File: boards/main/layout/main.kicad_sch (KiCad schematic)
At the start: 31 parts, among them IC1 STM32H725RGV6, P1 BM05B-SRSS-TB(LF)(SN)

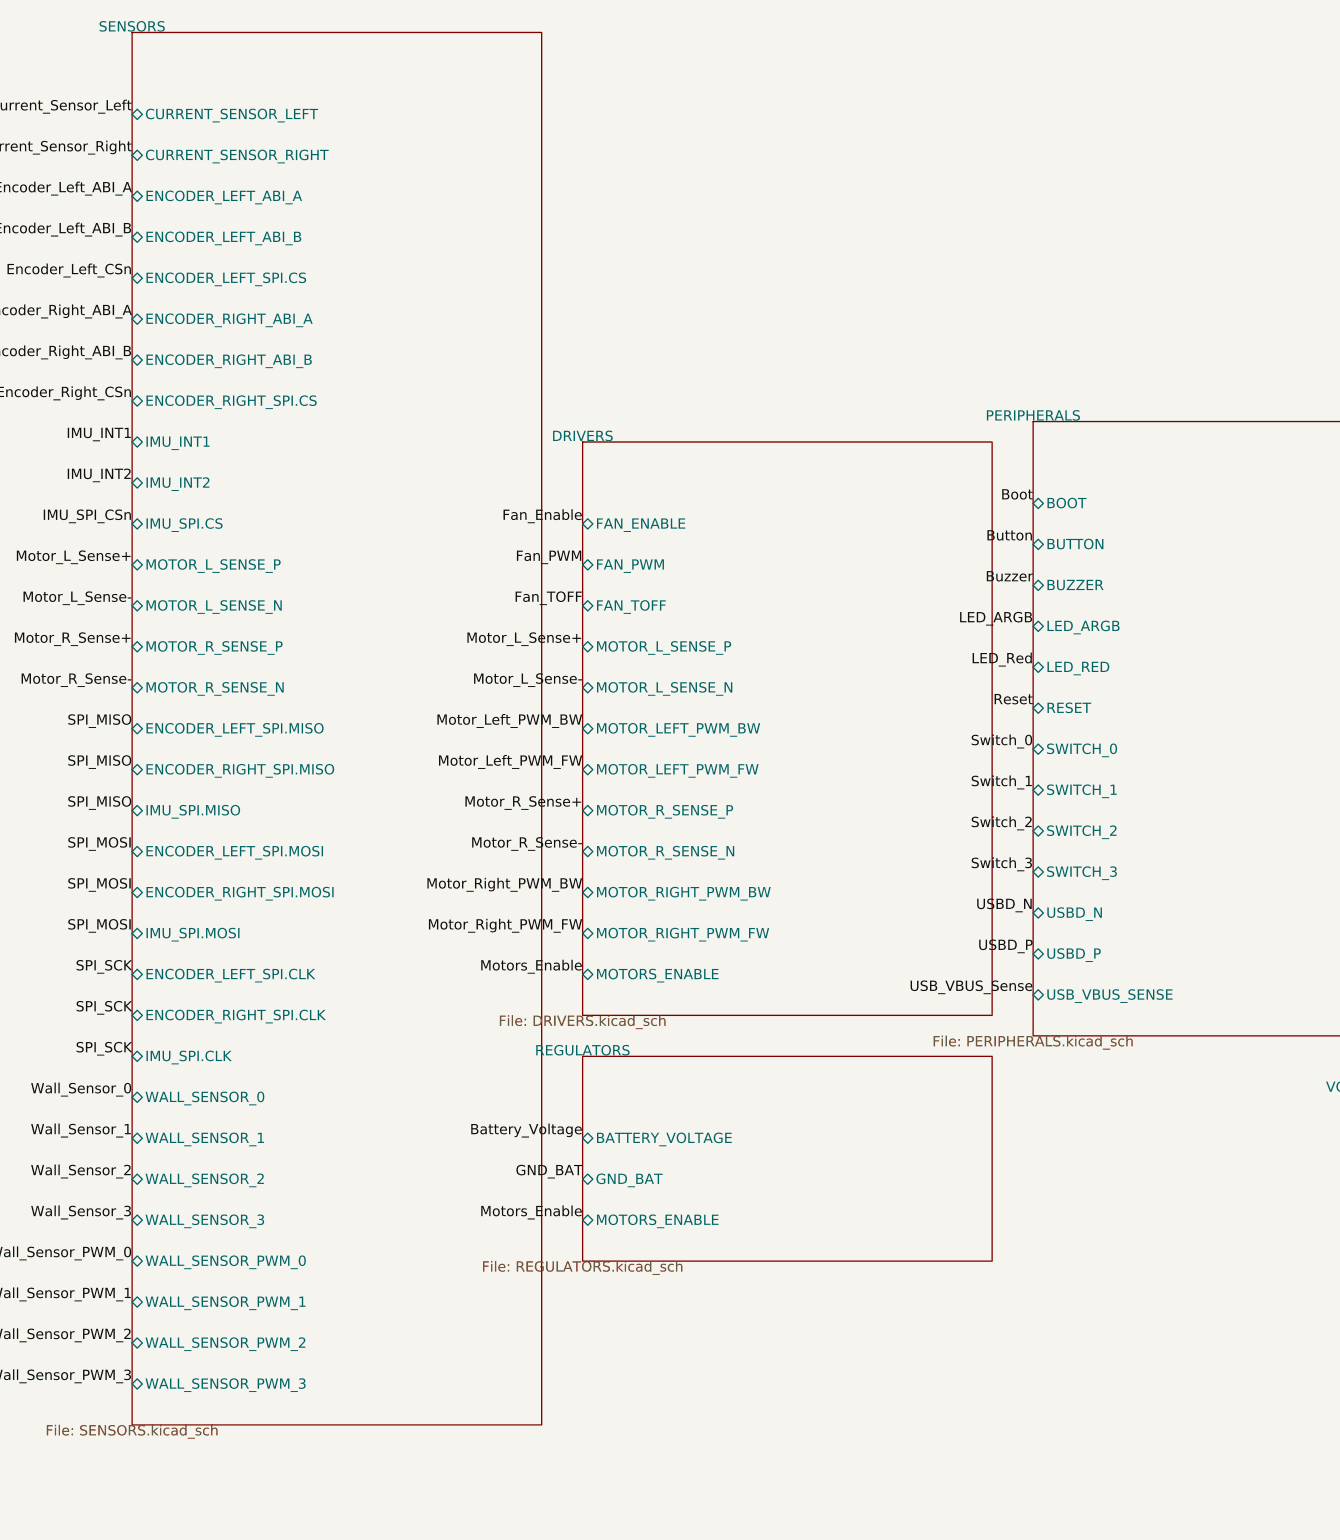
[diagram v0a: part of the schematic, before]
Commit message: 🏷️ Name the main board's module ports after their nets
A sheet pin and its hierarchical label take the module's port name and the root's label the net
name; KiCad's ERC flagged the 33 nets whose two names differed only in case (similar_labels).
GND_BAT becomes a ground port of REGULATORS, so the root shows a power symbol at its sheet pin
instead of a label nothing else joined (label_dangling).
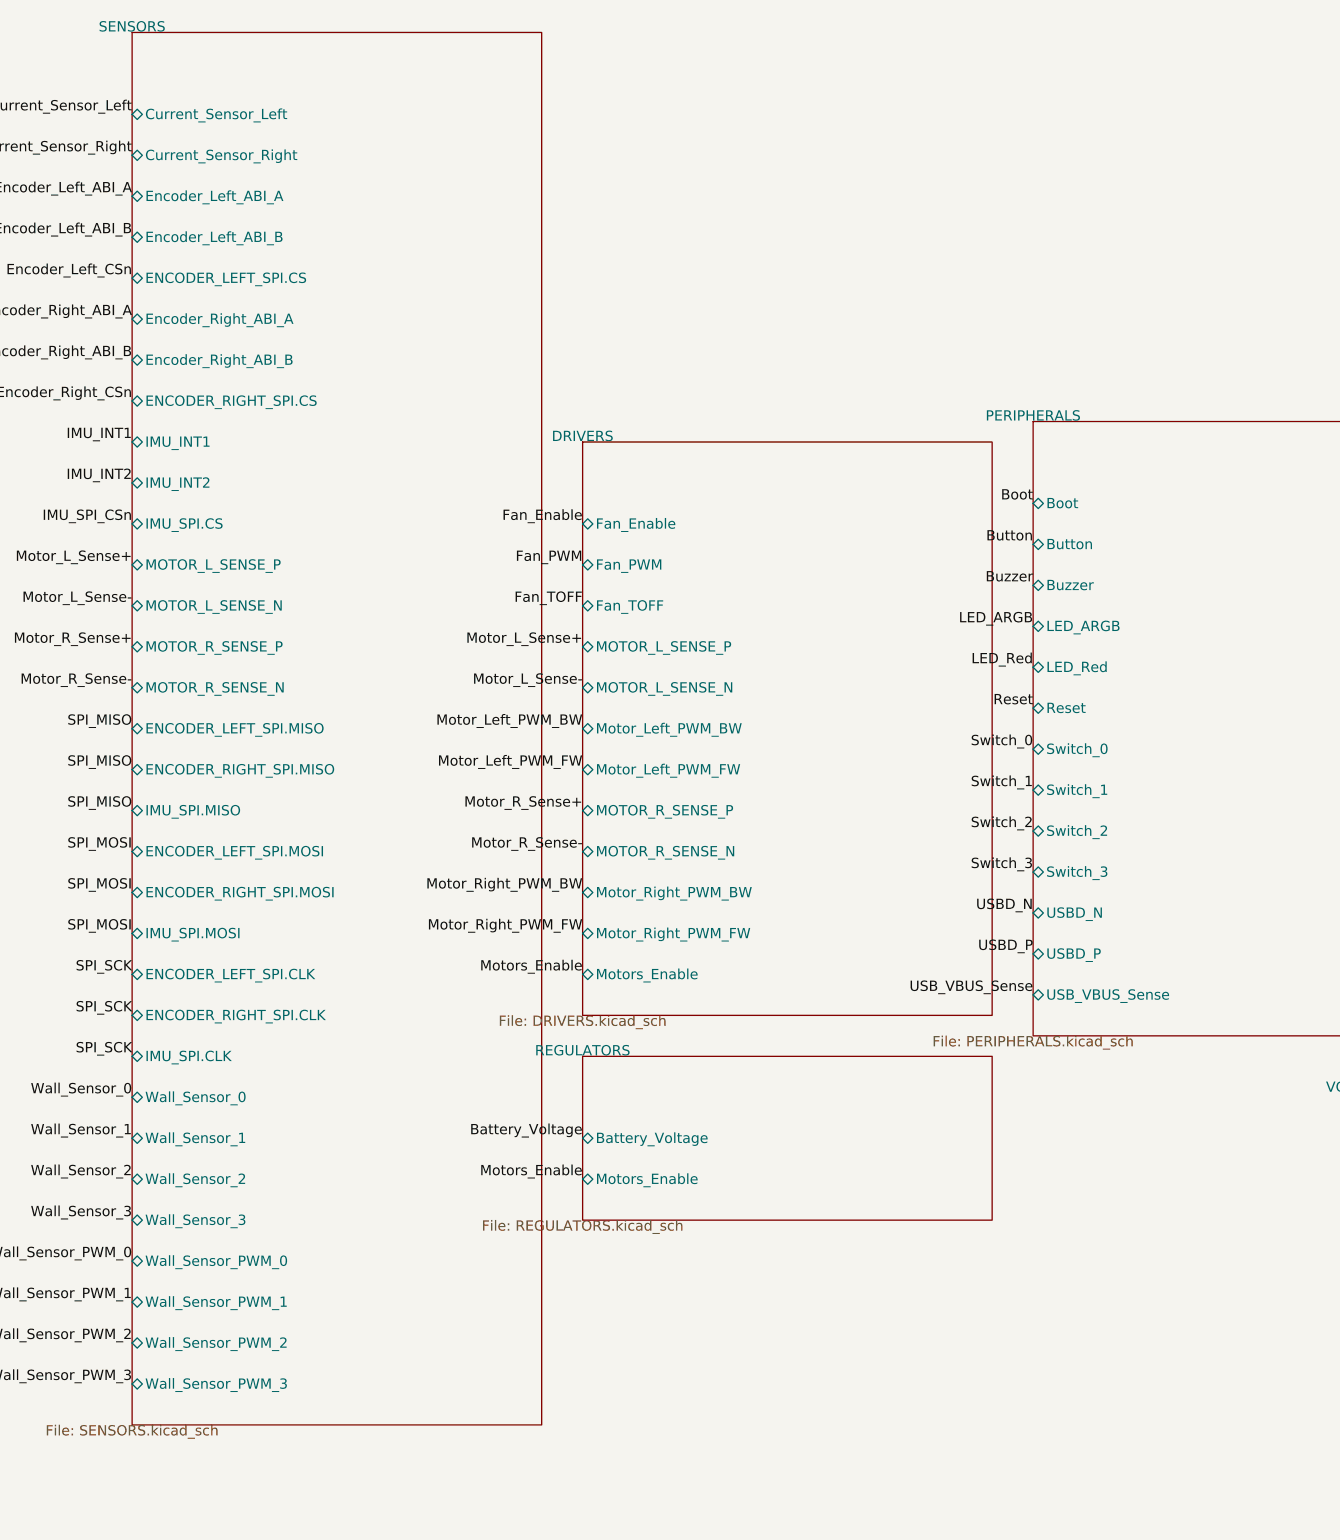
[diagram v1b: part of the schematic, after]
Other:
- sheet DRIVERS ports: added Fan_Enable, Fan_PWM, Fan_TOFF, Motor_Left_PWM_BW, Motor_Left_PWM_FW, Motor_Right_PWM_BW, Motor_Right_PWM_FW, Motors_Enable; removed FAN_ENABLE, FAN_PWM, FAN_TOFF, MOTORS_ENABLE, MOTOR_LEFT_PWM_BW, MOTOR_LEFT_PWM_FW, MOTOR_RIGHT_PWM_BW, MOTOR_RIGHT_PWM_FW
- sheet PERIPHERALS ports: added Boot, Button, Buzzer, LED_Red, Reset, Switch_0, Switch_1, Switch_2, Switch_3, USB_VBUS_Sense; removed BOOT, BUTTON, BUZZER, LED_RED, RESET, SWITCH_0, SWITCH_1, SWITCH_2, SWITCH_3, USB_VBUS_SENSE
- sheet REGULATORS ports: added Battery_Voltage, Motors_Enable; removed BATTERY_VOLTAGE, GND_BAT, MOTORS_ENABLE
- sheet SENSORS ports: added Current_Sensor_Left, Current_Sensor_Right, Encoder_Left_ABI_A, Encoder_Left_ABI_B, Encoder_Right_ABI_A, Encoder_Right_ABI_B, Wall_Sensor_0, Wall_Sensor_1, Wall_Sensor_2, Wall_Sensor_3, Wall_Sensor_PWM_0, Wall_Sensor_PWM_1, Wall_Sensor_PWM_2, Wall_Sensor_PWM_3; removed CURRENT_SENSOR_LEFT, CURRENT_SENSOR_RIGHT, ENCODER_LEFT_ABI_A, ENCODER_LEFT_ABI_B, ENCODER_RIGHT_ABI_A, ENCODER_RIGHT_ABI_B, WALL_SENSOR_0, WALL_SENSOR_1, WALL_SENSOR_2, WALL_SENSOR_3, WALL_SENSOR_PWM_0, WALL_SENSOR_PWM_1, WALL_SENSOR_PWM_2, WALL_SENSOR_PWM_3

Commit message: 🎨 Place the main board's root sheet: the MCU with its Direct SMPS supply, debug, test pads and the module sheets
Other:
- note added: "- No HSE or LSE crystal: PC15 and PH1 are unused."
- note added: "- VDD, VDDSMPS and VBAT on 3V3 (no backup battery)."
- note added: "- VDDA is also VREF+ on this package: FB1 keeps the"
- note added: "- VLXSMPS drives L1; VFBSMPS and VCAP1-3 all on VCORE."
- note added: "100 nF per VDD pin"
- note added: "C8, C9 at VBAT; C17 bulk"
- note added: "Direct SMPS supply (DS13311; AN5419 Table 2, Figure 5):"
- note added: "MCU: STM32H725RGV6, Direct SMPS supply and decoupling"
- note added: "Module sheets"
- note added: "Mounting holes (M2)"
- note added: "SWD debug connector"
- note added: "Test points (bare pads)"
- note added: "The firmware selects PWR_DIRECT_SMPS_SUPPLY."
- note added: "VCORE from the SMPS: 2 x 10 uF at L1, 100 nF per VCAP"
- note added: "VDDA = VREF+, filtered for the ADC"
- note added: "VDDSMPS: 10 uF + 4.7 uF"
- note added: "wall-emitter pulses on 3V3 out of the ADC reference."
- title: (none) -> MCU, debug and module sheets
- moved on the sheet: 20V1, C1, C10, C11, C12, C13, C14, C15, C16, C17, C2, C3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
